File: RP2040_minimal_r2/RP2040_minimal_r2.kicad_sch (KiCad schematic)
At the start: 34 parts, among them J1 USB_B_Micro, J2 Conn_01x02, J3 Conn_02x18_Odd_Even, J4 Conn_02x18_Odd_Even, U1 NCP1117-3.3_SOT223, U2 W25Q128JVS, U3 RP2040, Y1 ABM8-272-T3

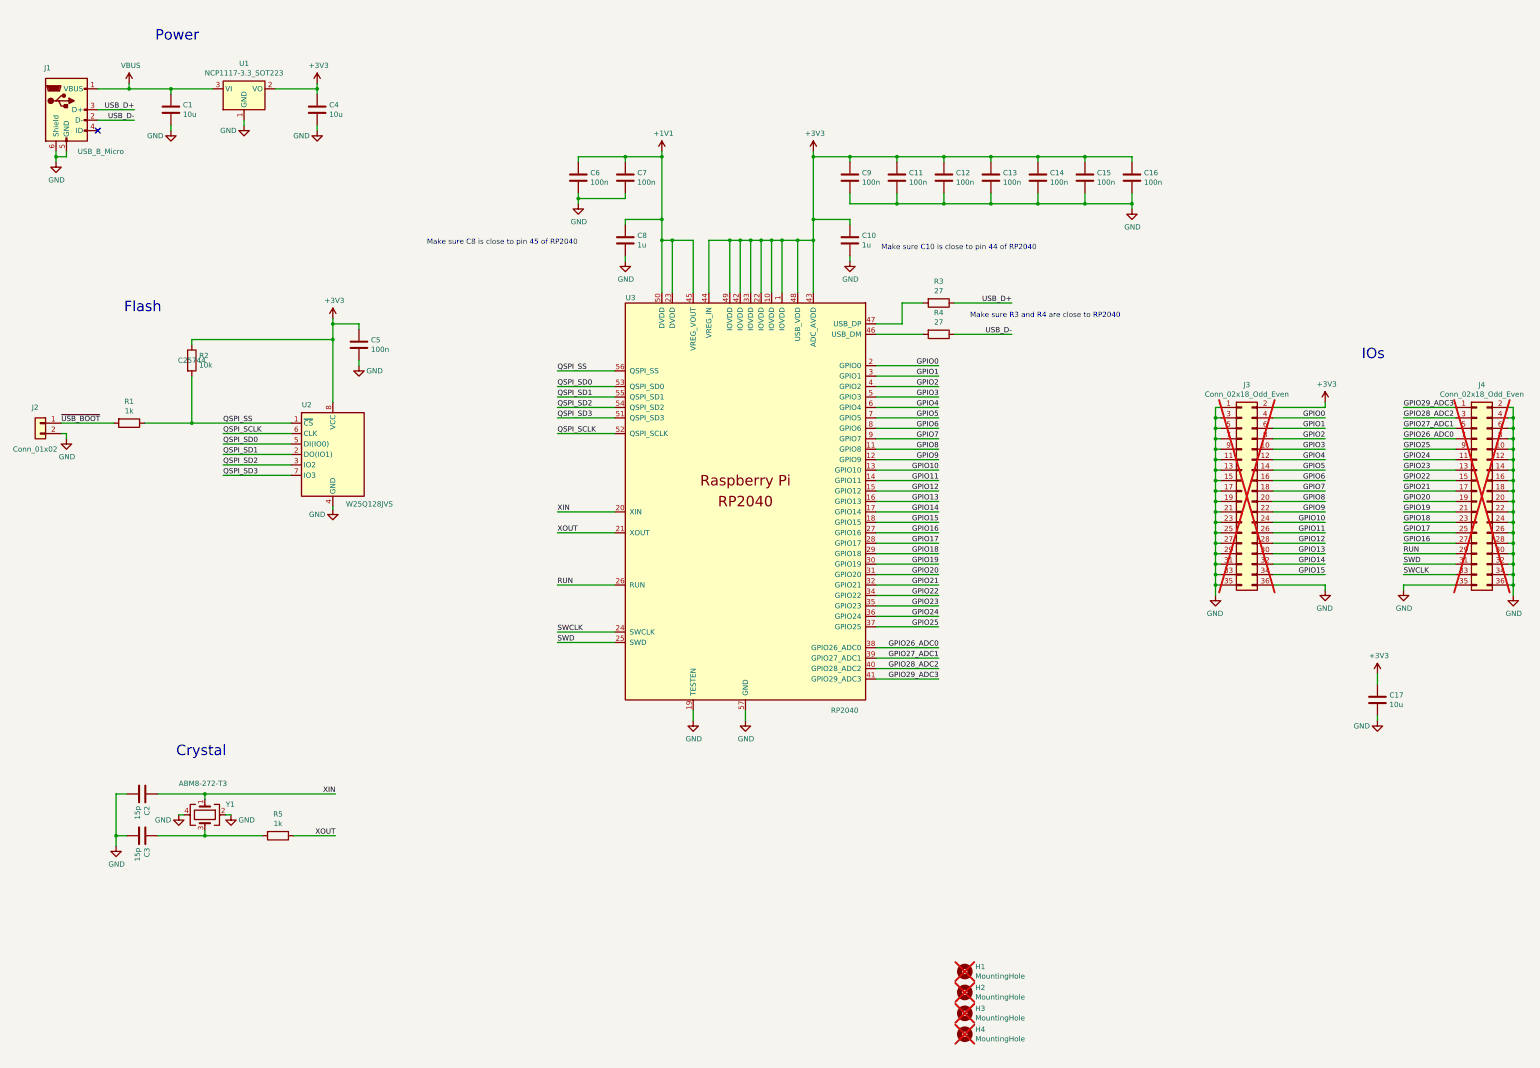
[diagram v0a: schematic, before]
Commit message: Reshape board to 46x34mm to match the footprint of the old breadboard. Replace some components (voltage regulator, flash memory chip, crystal) with ones that are cheaper and/or smaller Add BOOT/RESET buttons Add SMD piezo speaker add 3 SPI connectors (JST-GH 1.25mm pitch 6 pin). Lots of routing etc.
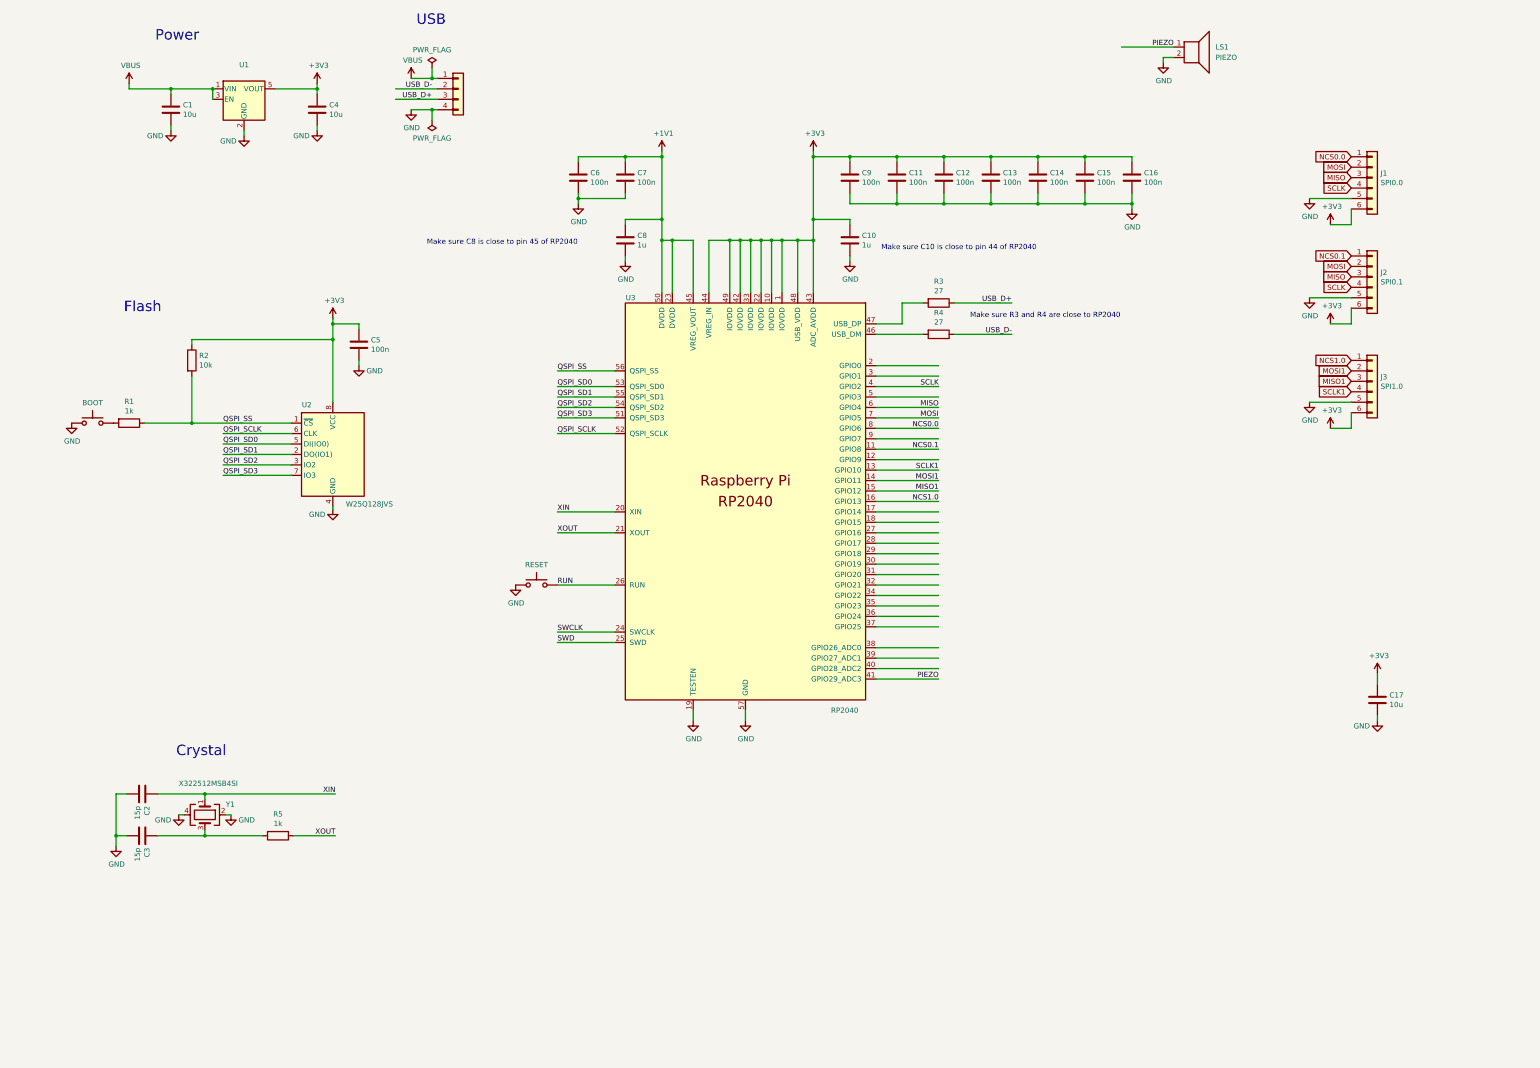
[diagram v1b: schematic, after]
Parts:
- removed H1, H2, H3, H4: MountingHole, MountingHole:MountingHole_2.7mm_M2.5, symbol Mechanical:MountingHole
- removed J1: USB_B_Micro, RP2040_minimal:USB_Micro-B_Amphenol_10103594-0001LF_Horizontal_modified, symbol Connector:USB_B_Micro
- removed J2: Conn_01x02, Connector_PinHeader_2.54mm:PinHeader_1x02_P2.54mm_Vertical, symbol Connector_Generic:Conn_01x02
- removed J3, J4: Conn_02x18_Odd_Even, Connector_PinHeader_2.54mm:PinHeader_2x18_P2.54mm_Vertical, symbol Connector_Generic:Conn_02x18_Odd_Even
- added J1: SPI0.0, Connector_JST:JST_GH_BM06B-GHS-TBT_1x06-1MP_P1.25mm_Vertical, symbol Connector_Generic:Conn_01x06
- added J2: SPI0.1, Connector_JST:JST_GH_BM06B-GHS-TBT_1x06-1MP_P1.25mm_Vertical, symbol Connector_Generic:Conn_01x06
- added J3: SPI1.0, Connector_JST:JST_GH_BM06B-GHS-TBT_1x06-1MP_P1.25mm_Vertical, symbol Connector_Generic:Conn_01x06
- added J5: USB, Connector_PinHeader_2.54mm:PinHeader_1x04_P2.54mm_Vertical, symbol Connector_Generic:Conn_01x04
- added LS1: PIEZO, Buzzer_Beeper:Buzzer_Murata_PKMCS0909E, symbol Device:Speaker
- added SW1: BOOT, Button_Switch_SMD:SW_SPST_B3U-1000P, symbol Switch:SW_Push
- added SW2: RESET, Button_Switch_SMD:SW_SPST_B3U-1000P, symbol Switch:SW_Push
- U1: value NCP1117-3.3_SOT223 -> AP2112K-3.3TRG1; footprint Package_TO_SOT_SMD:SOT-223-3_TabPin2 -> Package_TO_SOT_SMD:SOT-23-5; symbol Regulator_Linear:NCP1117-3.3_SOT223 -> Regulator_Linear:AP2112K-3.3; LCSC C26537 -> C51118
- U2: footprint Package_SO:SOIC-8_5.23x5.23mm_P1.27mm -> Package_SON:WSON-8-1EP_6x5mm_P1.27mm_EP3.4x4.3mm; symbol Memory_Flash:W25Q128JVS -> Memory_Flash:W25Q128JVP
- Y1: value ABM8-272-T3 -> X322512MSB4SI; LCSC C20625731 -> C9002
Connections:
- net +3V3: now also U1.5 (VOUT), J1.6 (Pin_6), J2.6 (Pin_6), J3.6 (Pin_6); no longer U1.2 (VO)
- net GND: now also U1.2 (GND), J1.5 (Pin_5), J2.5 (Pin_5), J3.5 (Pin_5), J5.4 (Pin_4), LS1.2, SW1.1, SW2.1; no longer U1.1 (GND)
- net RUN: now also SW2.2
- net USB_D+: now also J5.3 (Pin_3)
- net USB_D-: now also J5.2 (Pin_2)
- net VBUS: now also U1.1 (VIN), J5.1 (Pin_1)
- net GPIO0: no longer names the net of U3.2 (GPIO0)
- net GPIO1: no longer names the net of U3.3 (GPIO1)
- net GPIO10 renamed SCLK1
- net SCLK1: now also J3.4 (Pin_4)
- net GPIO11 renamed MOSI1
- net MOSI1: now also J3.2 (Pin_2)
- net GPIO12 renamed MISO1
- net MISO1: now also J3.3 (Pin_3)
- net GPIO13 renamed NCS1.0
- net NCS1.0: now also J3.1 (Pin_1)
- net GPIO14: no longer names the net of U3.17 (GPIO14)
- net GPIO15: no longer names the net of U3.18 (GPIO15)
- net GPIO16: no longer names the net of U3.27 (GPIO16)
- net GPIO17: no longer names the net of U3.28 (GPIO17)
- net GPIO18: no longer names the net of U3.29 (GPIO18)
- net GPIO19: no longer names the net of U3.30 (GPIO19)
- net GPIO2 renamed SCLK
- net SCLK: now also J1.4 (Pin_4), J2.4 (Pin_4)
- net GPIO20: no longer names the net of U3.31 (GPIO20)
- net GPIO21: no longer names the net of U3.32 (GPIO21)
- net GPIO22: no longer names the net of U3.34 (GPIO22)
- net GPIO23: no longer names the net of U3.35 (GPIO23)
- net GPIO24: no longer names the net of U3.36 (GPIO24)
- net GPIO25: no longer names the net of U3.37 (GPIO25)
- net GPIO26_ADC0: no longer names the net of U3.38 (GPIO26_ADC0)
- net GPIO27_ADC1: no longer names the net of U3.39 (GPIO27_ADC1)
- net GPIO28_ADC2: no longer names the net of U3.40 (GPIO28_ADC2)
- net GPIO29_ADC3 renamed PIEZO
- net PIEZO: now also LS1.1
- net GPIO3: no longer names the net of U3.5 (GPIO3)
- net GPIO4 renamed MISO
- net MISO: now also J1.3 (Pin_3), J2.3 (Pin_3)
- net GPIO5 renamed MOSI
- net MOSI: now also J1.2 (Pin_2), J2.2 (Pin_2)
- net GPIO6 renamed NCS0.0
- net NCS0.0: now also J1.1 (Pin_1)
- net GPIO7: no longer names the net of U3.9 (GPIO7)
- net GPIO8 renamed NCS0.1
- net NCS0.1: now also J2.1 (Pin_1)
- net GPIO9: no longer names the net of U3.12 (GPIO9)
- net ~{USB_BOOT}: no longer names the net of R1.2
- net ~{USB_BOOT}: now also SW1.2
- no-connect marks 1 -> 0
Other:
- note added: "USB"
- note removed: "IOs"

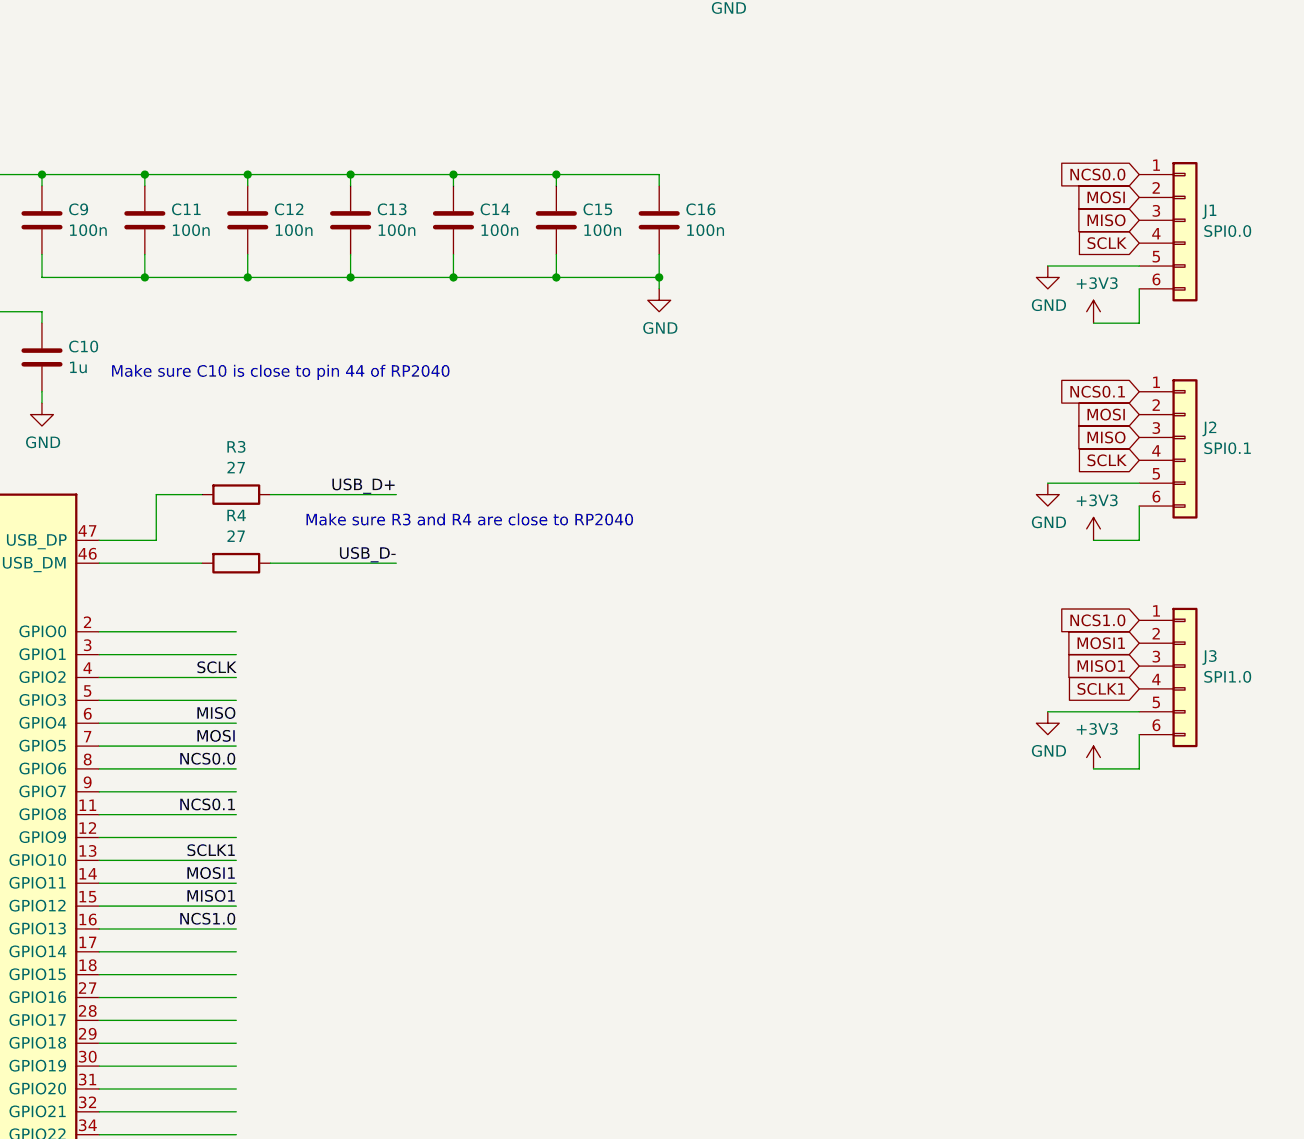
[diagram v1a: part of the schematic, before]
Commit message: Change connectors to JST-SH 1.0mm Additional routing tweaks.
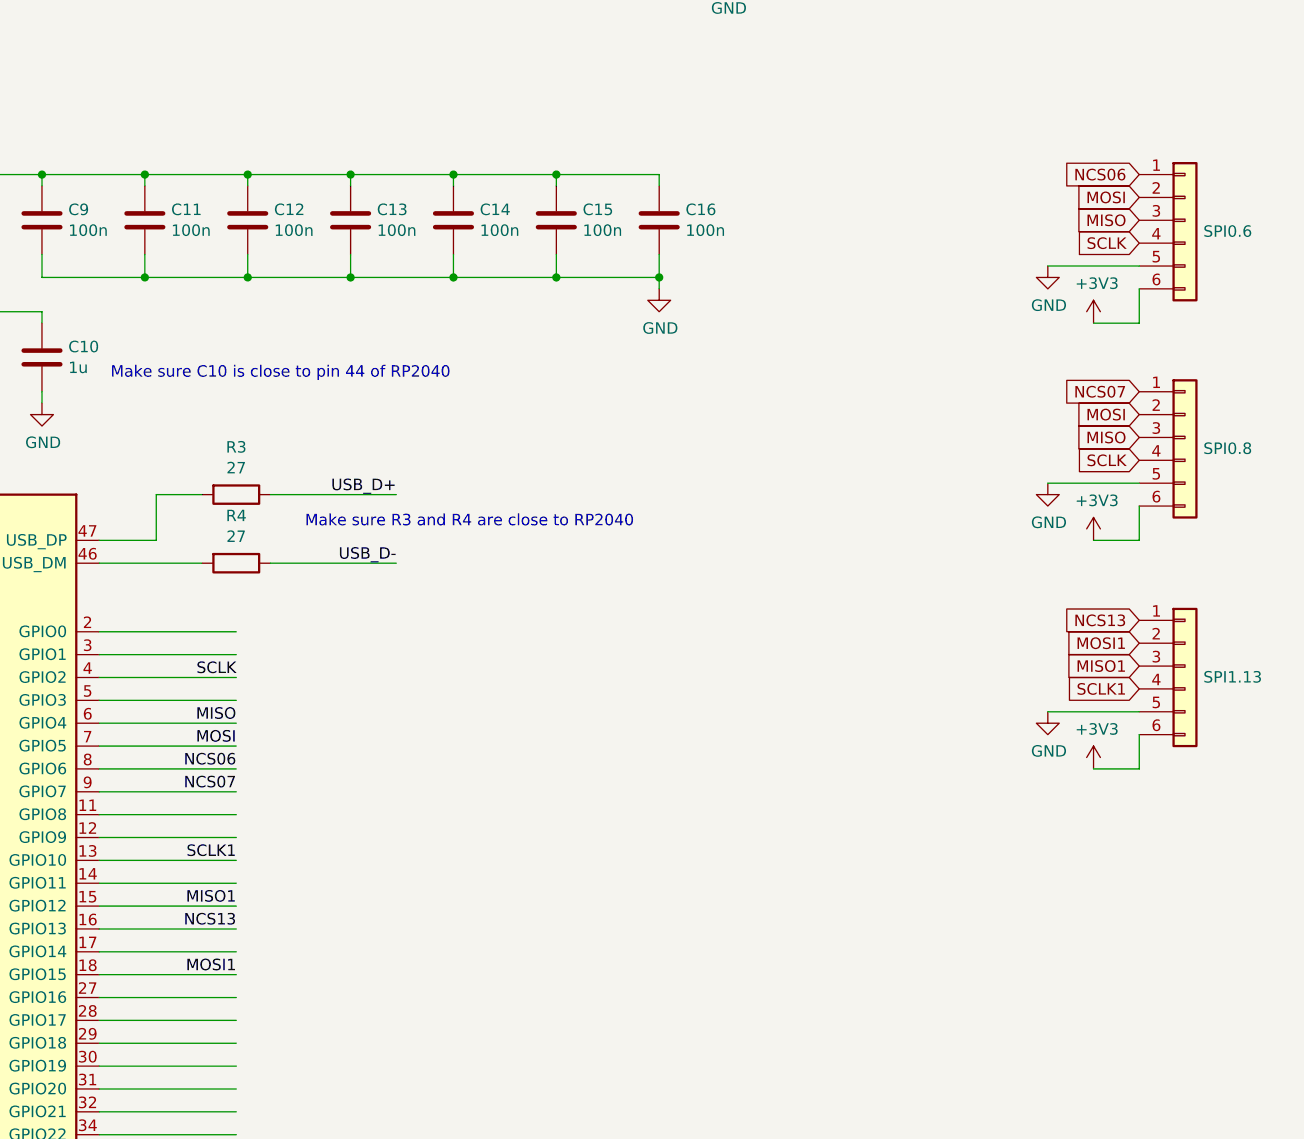
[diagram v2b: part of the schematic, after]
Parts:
- J1: value SPI0.0 -> SPI0.6; footprint Connector_JST:JST_GH_BM06B-GHS-TBT_1x06-1MP_P1.25mm_Vertical -> Connector_JST:JST_SH_BM06B-SRSS-TB_1x06-1MP_P1.00mm_Vertical; LCSC (none) -> C160392
- J2: value SPI0.1 -> SPI0.8; footprint Connector_JST:JST_GH_BM06B-GHS-TBT_1x06-1MP_P1.25mm_Vertical -> Connector_JST:JST_SH_BM06B-SRSS-TB_1x06-1MP_P1.00mm_Vertical; LCSC (none) -> C160392
- J3: value SPI1.0 -> SPI1.13; footprint Connector_JST:JST_GH_BM06B-GHS-TBT_1x06-1MP_P1.25mm_Vertical -> Connector_JST:JST_SH_BM06B-SRSS-TB_1x06-1MP_P1.00mm_Vertical; LCSC (none) -> C160392
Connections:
- net MOSI1: now also U3.18 (GPIO15); no longer U3.14 (GPIO11)
- net NCS07: now reaches U3.9 (GPIO7)
- net NCS07: now also J2.1 (Pin_1)
- net NCS0.0 renamed NCS06
- net NCS0.1: no longer names the net of U3.11 (GPIO8)
- net NCS0.1: no longer J2.1 (Pin_1)
- net NCS1.0 renamed NCS13
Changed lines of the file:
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@@
 		)
 	)
-	(label "NCS0.1"
-		(at 245.11 132.08 180)
-		(fields_autoplaced yes)
-		(effects
-			(font
-				(size 1.27 1.27)
-			)
-			(justify right bottom)
-		)
-	)
 	(label "RUN"
 		(at 152.4 165.1 0)
@@
 		)
 	)
-	(label "NCS1.0"
+	(label "NCS13"
 		(at 245.11 144.78 180)
 		(fields_autoplaced yes)
@@
 		)
 	)
-	(label "NCS0.0"
+	(label "NCS06"
 		(at 245.11 127 180)
 		(fields_autoplaced yes)
@@
 		)
 	)
-	(label "MOSI1"
-		(at 245.11 139.7 180)
-		(fields_autoplaced yes)
-		(effects
-			(font
-				(size 1.27 1.27)
-			)
-			(justify right bottom)
-		)
-	)
 	(label "XIN"
 		(at 98.425 215.9 180)
@@
 		)
 	)
+	(label "MOSI1"
+		(at 245.11 149.86 180)
+		(fields_autoplaced yes)
+		(effects
+			(font
+				(size 1.27 1.27)
+			)
+			(justify right bottom)
+		)
+	)
 	(label "QSPI_SCLK"
 		(at 152.4 128.27 0)
@@
 		)
 	)
+	(label "NCS07"
+		(at 245.11 129.54 180)
+		(fields_autoplaced yes)
+		(effects
+			(font
+				(size 1.27 1.27)
+			)
+			(justify right bottom)
+		)
+	)
 	(global_label "MOSI"
 		(shape input)
@@
 		)
 	)
-	(global_label "NCS1.0"
+	(global_label "NCS13"
 		(shape input)
 		(at 345.44 110.49 180)
@@
 		)
 	)
-	(global_label "NCS0.1"
+	(global_label "NCS07"
 		(shape input)
 		(at 345.44 85.09 180)
@@
 		)
 	)
-	(global_label "NCS0.0"
+	(global_label "NCS06"
 		(shape input)
 		(at 345.44 60.96 180)
@@
 				)
 				(justify left)
+				(hide yes)
 			)
 		)
-		(property "Value" "SPI0.1"
+		(property "Value" "SPI0.8"
 			(at 352.552 91.4146 0)
 			(effects
@@
 			)
 		)
-		(property "Footprint" "Connector_JST:JST_GH_BM06B-GHS-TBT_1x06-1MP_P1.25mm_Vertical"
+		(property "Footprint" "Connector_JST:JST_SH_BM06B-SRSS-TB_1x06-1MP_P1.00mm_Vertical"
 			(at 350.52 90.17 0)
 			(effects
@@
 			)
 		)
-		(property "Datasheet" "~"
+		(property "Datasheet" "https://www.lcsc.com/datasheet/lcsc_datasheet_2304140030_JST-BM06B-SRSS-TB-LF-SN_C160392.pdf"
 			(at 350.52 90.17 0)
 			(effects
@@
 			)
 		)
+		(property "LCSC" "C160392"
+			(at 350.52 90.17 0)
+			(effects
+				(font
+					(size 1.27 1.27)
+				)
+				(hide yes)
+			)
+		)
 		(pin "4"
 		)
@@
 				)
 				(justify left)
+				(hide yes)
 			)
 		)
-		(property "Value" "SPI1.0"
+		(property "Value" "SPI1.13"
 			(at 352.552 116.8146 0)
 			(effects
@@
 			)
 		)
-		(property "Footprint" "Connector_JST:JST_GH_BM06B-GHS-TBT_1x06-1MP_P1.25mm_Vertical"
+		(property "Footprint" "Connector_JST:JST_SH_BM06B-SRSS-TB_1x06-1MP_P1.00mm_Vertical"
 			(at 350.52 115.57 0)
 			(effects
@@
 			)
 		)
-		(property "Datasheet" "~"
+		(property "Datasheet" "https://www.lcsc.com/datasheet/lcsc_datasheet_2304140030_JST-BM06B-SRSS-TB-LF-SN_C160392.pdf"
 			(at 350.52 115.57 0)
 			(effects
@@
 			)
 		)
+		(property "LCSC" "C160392"
+			(at 350.52 115.57 0)
+			(effects
+				(font
+					(size 1.27 1.27)
+				)
+				(hide yes)
+			)
+		)
 		(pin "4"
 		)
@@
 				)
 				(justify left)
+				(hide yes)
 			)
 		)
-		(property "Value" "SPI0.0"
+		(property "Value" "SPI0.6"
 			(at 352.552 67.2846 0)
 			(effects
@@
 			)
 		)
-		(property "Footprint" "Connector_JST:JST_GH_BM06B-GHS-TBT_1x06-1MP_P1.25mm_Vertical"
+		(property "Footprint" "Connector_JST:JST_SH_BM06B-SRSS-TB_1x06-1MP_P1.00mm_Vertical"
 			(at 350.52 66.04 0)
 			(effects
@@
 			)
 		)
-		(property "Datasheet" "~"
+		(property "Datasheet" "https://www.lcsc.com/datasheet/lcsc_datasheet_2304140030_JST-BM06B-SRSS-TB-LF-SN_C160392.pdf"
 			(at 350.52 66.04 0)
 			(effects
@@
 			(at 350.52 66.04 0)
 			(effects
+				(font
+					(size 1.27 1.27)
+				)
+				(hide yes)
+			)
+		)
+		(property "LCSC" "C160392"
+			(at 350.52 66.04 0)
+			(effects
